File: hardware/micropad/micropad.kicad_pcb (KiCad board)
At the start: 2 copper layers, 45.1 x 76.5 mm, 29 parts, among them J2 Conn_ARM_JTAG_SWD_10, J3 USB_B_Micro, SW1 SW_SPST, SW2 SW_SPST, SW3 SW_SPST, U1 LD1117S33TR_SOT223, U2 STM32F042K6Ux, U3 APA102

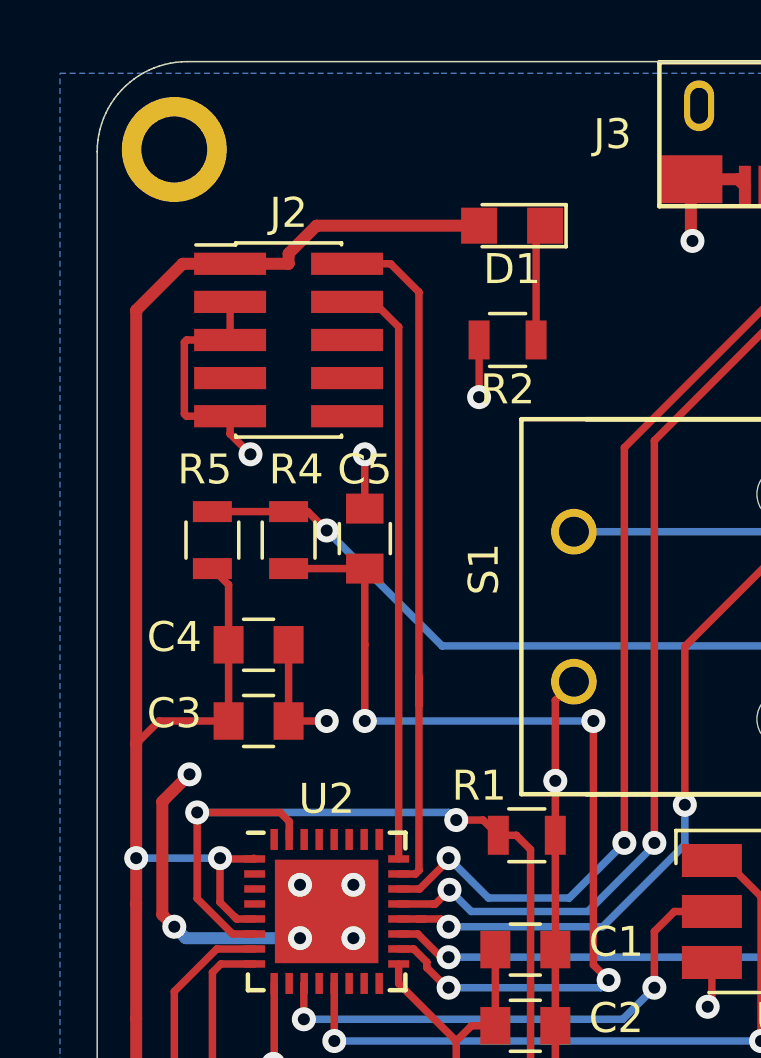
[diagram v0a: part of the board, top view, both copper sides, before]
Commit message: Use temporary connector for SWD programming
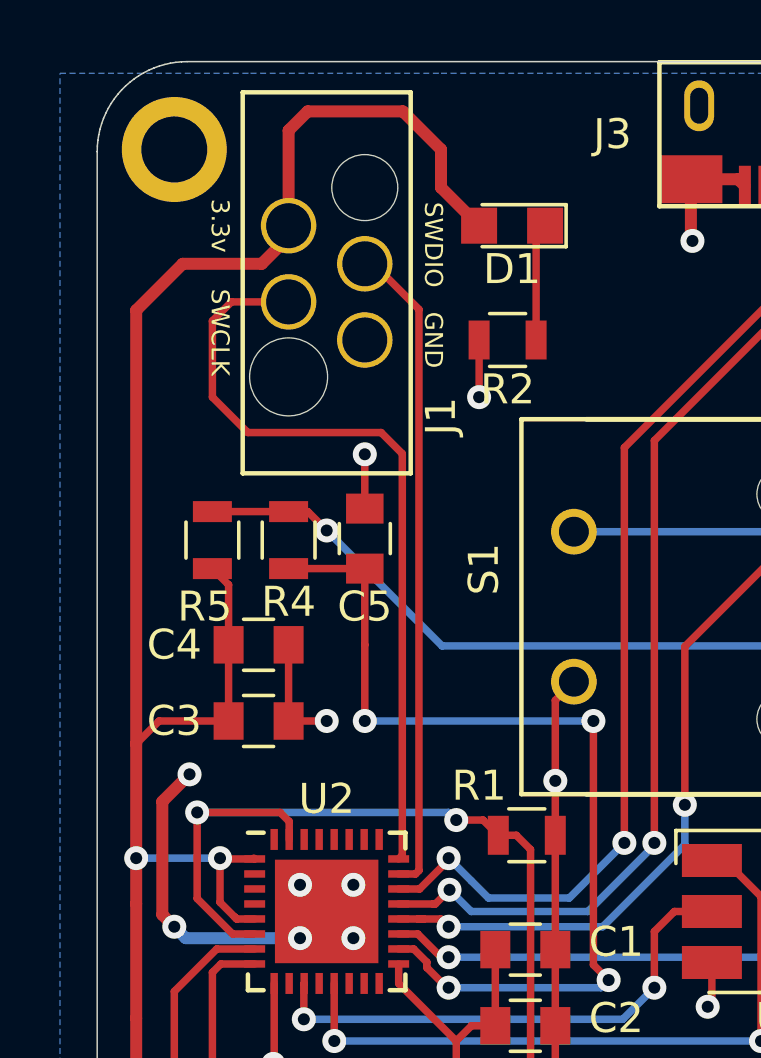
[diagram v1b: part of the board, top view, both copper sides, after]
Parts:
- removed J2: Conn_ARM_JTAG_SWD_10, Pin_Headers:Pin_Header_Straight_2x05_Pitch1.27mm_SMD
- added J1: SWD Debug, micropad:REDFIT_IDC_SKEDD_CONN_4PIN, F.Cu at (38.1, 29.8)
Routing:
- net GND: track 57.3 -> 49.0 mm, vias 18 -> 17
- net /SWCLK: track 19.8 -> 26.0 mm
- net +3V3: track 235.3 -> 241.1 mm
- net /SWDIO: track 23.7 -> 21.5 mm
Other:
- board text added: "3.3v"
- board text added: "GND"
- board text added: "SWCLK"
- board text added: "SWDIO"

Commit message: Add logo
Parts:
- added G***: LOGO, micropad:square_only, F.Cu at (70.5, 31.8)
- added G***: LOGO, micropad:logo, B.Cu at (52.8, 70.1)
- added REF***: OSHW-Logo2_7.3x6mm_SilkScreen, Symbols:OSHW-Logo2_7.3x6mm_SilkScreen, F.Cu at (38.7, 90.2)
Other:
- board text added: "micropad rev. 1"

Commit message: Fixup DRC
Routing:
- net /LED_USR: track 35.7 -> 37.6 mm
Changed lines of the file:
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@@
     (thickness 1.6)
     (drawings 525)
-    (tracks 282)
+    (tracks 283)
     (zones 0)
     (modules 32)
@@
   (segment (start 57.215153 34.224847) (end 55.88 35.56) (width 0.25) (layer B.Cu) (net 6))
   (via (at 55.88 35.56) (size 0.8) (drill 0.4) (layers F.Cu B.Cu) (net 6))
-  (segment (start 50.038 41.967685) (end 50.038 47.244) (width 0.25) (layer F.Cu) (net 6))
-  (segment (start 55.88 36.125685) (end 50.038 41.967685) (width 0.25) (layer F.Cu) (net 6))
-  (segment (start 55.88 35.56) (end 55.88 36.125685) (width 0.25) (layer F.Cu) (net 6))
+  (segment (start 53.282315 41.967685) (end 55.88 39.37) (width 0.25) (layer F.Cu) (net 6))
+  (segment (start 50.038 41.967685) (end 53.282315 41.967685) (width 0.25) (layer F.Cu) (net 6))
+  (segment (start 55.88 39.37) (end 55.88 35.56) (width 0.25) (layer F.Cu) (net 6))
+  (segment (start 50.038 47.244) (end 50.038 41.967685) (width 0.25) (layer F.Cu) (net 6))
   (segment (start 61.91 28.09) (end 62.06 27.94) (width 0.25) (layer F.Cu) (net 7))
   (segment (start 61.91 31.75) (end 61.91 28.09) (width 0.25) (layer F.Cu) (net 7))
